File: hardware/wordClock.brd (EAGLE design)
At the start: 49.2 x 49.5 mm, 38 parts, among them J1 SPI_PRG, Q1 MOSFET-PCHANNELSMD, Q2 MOSFET-PCHANNELSMD, Q3 MOSFET-PCHANNELSMD, Q4 MOSFET-PCHANNELSMD, Q5 MOSFET-PCHANNELSMD, Q6 MOSFET-PCHANNELSMD, Q7 MOSFET-PCHANNELSMD, Q8 MOSFET-PCHANNELSMD, U2 TLC5940-NT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

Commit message: Fixed ERC errors and Fixed annotation breaks
Should be all good now, Got broken nets fixed, switched larger usb jack
for a micro.
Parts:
- C1: value (none) -> 10uF
- C2, C3, C4, C5, C8: value (none) -> .1uF
- C6, C7: value (none) -> 22uF
- JP1: value USB_PWR -> USB-MICROB; device SparkFun-Connectors:USB-B-PTH-VERTICAL -> SparkFun-Connectors:USB-MICROB
- SW1: value (none) -> HR
- SW2: value (none) -> MIN
- moved JP1 6.63 mm to (8.89, 3.17)
- renumbered HR to SW1, JP4 to COL, MIN to SW2, U$1 to ROW
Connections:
- removed net N$7: C6.2, C7.2, U3.21, U3.3, U3.5
- removed net ROW8: COL.9
- removed net ROW9: COL.10
- removed net SCI: U3.28
- net CE: now also U3.25
- net CLK: now also U3.12
- net GND: now also C6.2, C7.2, JP1.MT1, JP1.MT2, U3.21, U3.3, U3.5
- net IO: now also U3.26
- net SCL: now also U3.28
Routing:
- net N$7: track 5.08 -> 0.00 mm
- net GND: track 1.75 -> 6.83 mm

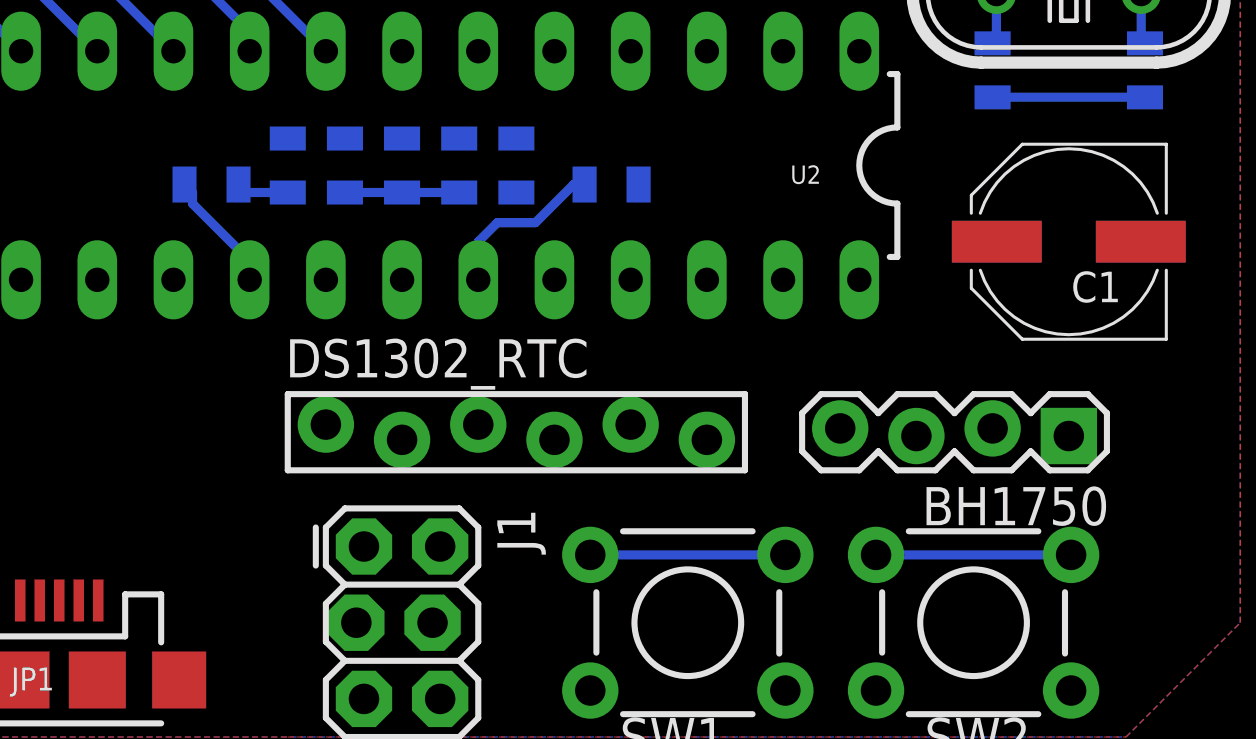
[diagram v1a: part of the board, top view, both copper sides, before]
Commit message: ALL ANNOTATION BREAKS FIXED
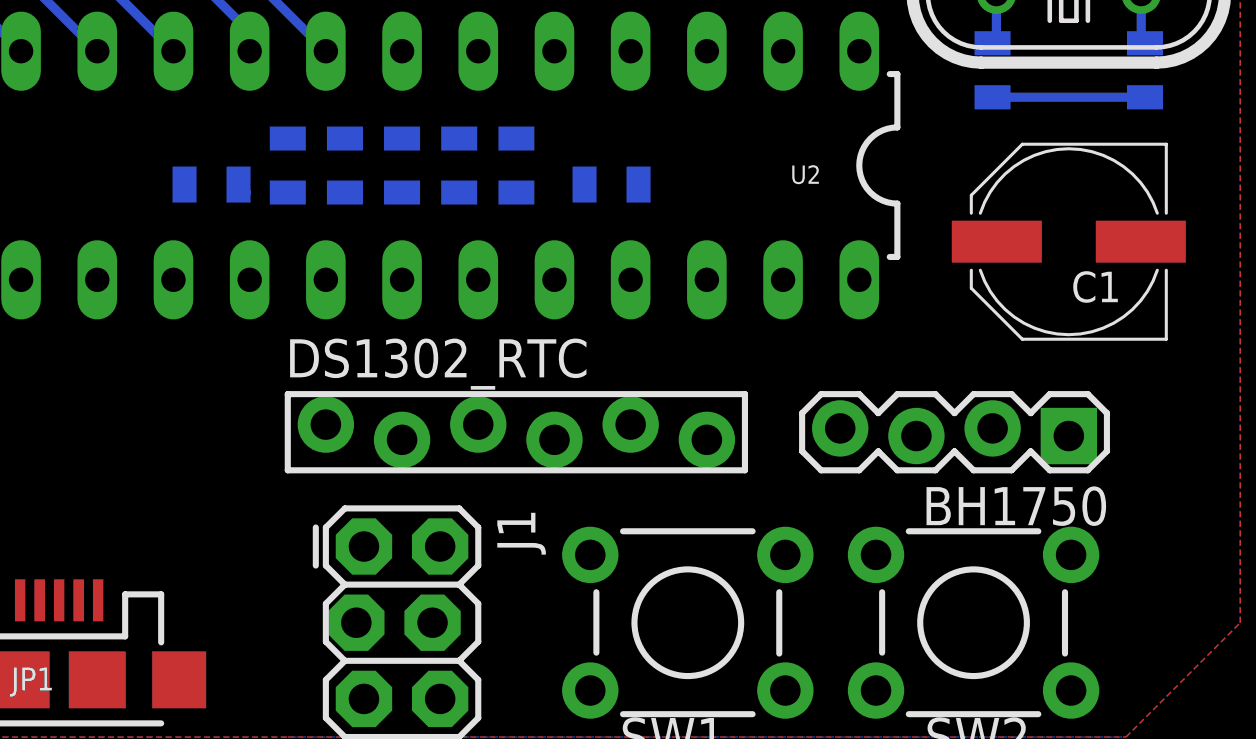
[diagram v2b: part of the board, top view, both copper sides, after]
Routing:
- net MIN: track 6.50 -> 0.00 mm
- net HR: track 6.50 -> 0.00 mm
- net BLANK: track 5.60 -> 0.00 mm
- net N$1: track 4.07 -> 0.00 mm
- net N$5: track 3.81 -> 0.00 mm
- net GND: track 6.83 -> 5.45 mm
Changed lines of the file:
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@@
 <vertex x="5.08" y="1.27"/>
 </polygon>
-<wire x1="16.51" y1="19.42" x2="15.135" y2="19.42" width="0.3048" layer="16"/>
+<wire x1="16.51" y1="19.42" x2="15.135" y2="19.42" width="0" layer="19" extent="1-16"/>
 <wire x1="15.135" y1="19.42" x2="14.87" y2="19.685" width="0.3048" layer="16"/>
 <contactref element="U3" pad="3"/>
@@
 <contactref element="R2" pad="1"/>
 <contactref element="U3" pad="14"/>
-<wire x1="26.405" y1="19.685" x2="26.035" y2="19.685" width="0.3048" layer="16"/>
-<wire x1="26.035" y1="19.685" x2="24.765" y2="18.415" width="0.3048" layer="16"/>
-<wire x1="24.765" y1="18.415" x2="23.495" y2="18.415" width="0.3048" layer="16"/>
-<wire x1="23.495" y1="18.415" x2="22.86" y2="17.78" width="0.3048" layer="16"/>
-<wire x1="22.86" y1="17.78" x2="22.86" y2="16.51" width="0.3048" layer="16"/>
-<wire x1="23.495" y1="18.415" x2="13.4874" y2="30.931" width="0" layer="19" extent="1-16"/>
+<wire x1="22.86" y1="16.51" x2="26.405" y2="19.685" width="0" layer="19" extent="16-16"/>
+<wire x1="13.4874" y1="30.931" x2="26.405" y2="19.685" width="0" layer="19" extent="1-16"/>
 </signal>
 <signal name="SIN">
@@
 <contactref element="SW1" pad="3"/>
 <contactref element="U3" pad="23"/>
-<wire x1="33.0962" y1="7.3406" x2="26.5938" y2="7.3406" width="0.3048" layer="16"/>
 <wire x1="26.5938" y1="7.3406" x2="19.78" y2="27.8384" width="0" layer="19" extent="1-1"/>
+<wire x1="33.0962" y1="7.3406" x2="26.5938" y2="7.3406" width="0" layer="19" extent="1-1"/>
 </signal>
 <signal name="MIN">
@@
 <contactref element="SW2" pad="3"/>
 <contactref element="U3" pad="24"/>
-<wire x1="42.6212" y1="7.3406" x2="36.1188" y2="7.3406" width="0.3048" layer="16"/>
-<wire x1="36.1188" y1="7.3406" x2="20.58" y2="27.8384" width="0" layer="19" extent="1-1"/>
+<wire x1="36.1188" y1="7.3406" x2="42.6212" y2="7.3406" width="0" layer="19" extent="1-1"/>
+<wire x1="20.58" y1="27.8384" x2="36.1188" y2="7.3406" width="0" layer="19" extent="1-1"/>
 </signal>
 <signal name="N$2">
@@
 <contactref element="U2" pad="20"/>
 <contactref element="R3" pad="1"/>
-<wire x1="15.24" y1="16.51" x2="15.24" y2="17.145" width="0.3048" layer="16"/>
-<wire x1="15.24" y1="17.145" x2="13.335" y2="19.05" width="0.3048" layer="16"/>
-<wire x1="13.335" y1="19.05" x2="13.335" y2="19.42" width="0.3048" layer="16"/>
-<wire x1="13.335" y1="19.42" x2="13.07" y2="19.685" width="0.3048" layer="16"/>
+<wire x1="13.07" y1="19.685" x2="15.24" y2="16.51" width="0" layer="19" extent="16-16"/>
 </signal>
 <signal name="MISO">
@@
 <wire x1="32.215" y1="40.005" x2="30.945" y2="41.275" width="0.3048" layer="16"/>
 </signal>
-<signal name="N$3">
+<signal name="N$5">
 <contactref element="C5" pad="2"/>
 <contactref element="C3" pad="2"/>
 <contactref element="C4" pad="2"/>
-<wire x1="18.415" y1="19.42" x2="20.32" y2="19.42" width="0.3048" layer="16"/>
-<wire x1="22.225" y1="19.42" x2="20.32" y2="19.42" width="0.3048" layer="16"/>
+<wire x1="20.32" y1="19.42" x2="22.225" y2="19.42" width="0" layer="19" extent="16-16"/>
+<wire x1="18.415" y1="19.42" x2="20.32" y2="19.42" width="0" layer="19" extent="16-16"/>
 </signal>
 </signals>

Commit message: Fixed floating nets
There was a floating net around the crystal, SCL was named SLI on a pin,
and various ERC errors fixed.
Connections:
- removed net N$5: C3.2, C4.2, C5.2
- net GND: now also C3.2, C4.2, C5.2
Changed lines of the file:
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@@
 <vertex x="5.08" y="1.27"/>
 </polygon>
-<wire x1="16.51" y1="19.42" x2="15.135" y2="19.42" width="0" layer="19" extent="1-16"/>
 <wire x1="15.135" y1="19.42" x2="14.87" y2="19.685" width="0.3048" layer="16"/>
 <contactref element="U3" pad="3"/>
@@
 <contactref element="JP1" pad="GND"/>
 <contactref element="JP1" pad="MT2"/>
+<contactref element="C5" pad="2"/>
+<contactref element="C3" pad="2"/>
+<contactref element="C4" pad="2"/>
 <wire x1="45.085" y1="22.595" x2="44.945" y2="17.78" width="0" layer="19" extent="1-16"/>
 <wire x1="40.005" y1="11.557" x2="44.945" y2="17.78" width="0" layer="19" extent="1-1"/>
@@
 <wire x1="26.5938" y1="2.8194" x2="33.0962" y2="2.8194" width="0" layer="19" extent="1-1"/>
 <wire x1="21.59" y1="2.54" x2="26.5938" y2="2.8194" width="0" layer="19" extent="1-1"/>
-<wire x1="22.86" y1="11.684" x2="21.59" y2="2.54" width="0" layer="19" extent="1-1"/>
-<wire x1="20.32" y1="16.51" x2="22.86" y2="11.684" width="0" layer="19" extent="1-1"/>
-<wire x1="24.13" y1="19.42" x2="20.32" y2="16.51" width="0" layer="19" extent="16-16"/>
-<wire x1="16.51" y1="19.42" x2="20.32" y2="16.51" width="0" layer="19" extent="16-16"/>
-<wire x1="18.18" y1="27.8384" x2="16.51" y2="19.42" width="0" layer="19" extent="1-16"/>
-<wire x1="18.98" y1="36.4236" x2="18.18" y2="27.8384" width="0" layer="19" extent="1-1"/>
-<wire x1="17.38" y1="36.4236" x2="18.98" y2="36.4236" width="0" layer="19" extent="1-1"/>
 <wire x1="12.89" y1="3.175" x2="21.59" y2="2.54" width="0" layer="19" extent="1-1"/>
 <wire x1="10.19" y1="5.825" x2="12.89" y2="3.175" width="0" layer="19" extent="1-1"/>
 <wire x1="4.89" y1="3.175" x2="10.19" y2="5.825" width="0" layer="19" extent="1-1"/>
+<wire x1="22.86" y1="11.684" x2="21.59" y2="2.54" width="0" layer="19" extent="1-1"/>
+<wire x1="20.32" y1="16.51" x2="22.86" y2="11.684" width="0" layer="19" extent="1-1"/>
+<wire x1="20.32" y1="19.42" x2="20.32" y2="16.51" width="0" layer="19" extent="16-16"/>
+<wire x1="22.225" y1="19.42" x2="20.32" y2="19.42" width="0" layer="19" extent="16-16"/>
+<wire x1="24.13" y1="19.42" x2="22.225" y2="19.42" width="0" layer="19" extent="16-16"/>
+<wire x1="18.415" y1="19.42" x2="20.32" y2="19.42" width="0" layer="19" extent="16-16"/>
+<wire x1="16.51" y1="19.42" x2="18.415" y2="19.42" width="0" layer="19" extent="16-16"/>
+<wire x1="15.135" y1="19.42" x2="16.51" y2="19.42" width="0" layer="19" extent="16-16"/>
+<wire x1="18.18" y1="27.8384" x2="18.415" y2="19.42" width="0" layer="19" extent="1-16"/>
+<wire x1="18.98" y1="36.4236" x2="18.18" y2="27.8384" width="0" layer="19" extent="1-1"/>
+<wire x1="17.38" y1="36.4236" x2="18.98" y2="36.4236" width="0" layer="19" extent="1-1"/>
 </signal>
 <signal name="CLK">
@@
 <wire x1="32.215" y1="40.005" x2="30.945" y2="41.275" width="0.3048" layer="16"/>
 </signal>
-<signal name="N$5">
-<contactref element="C5" pad="2"/>
-<contactref element="C3" pad="2"/>
-<contactref element="C4" pad="2"/>
-<wire x1="20.32" y1="19.42" x2="22.225" y2="19.42" width="0" layer="19" extent="16-16"/>
-<wire x1="18.415" y1="19.42" x2="20.32" y2="19.42" width="0" layer="19" extent="16-16"/>
-</signal>
 </signals>

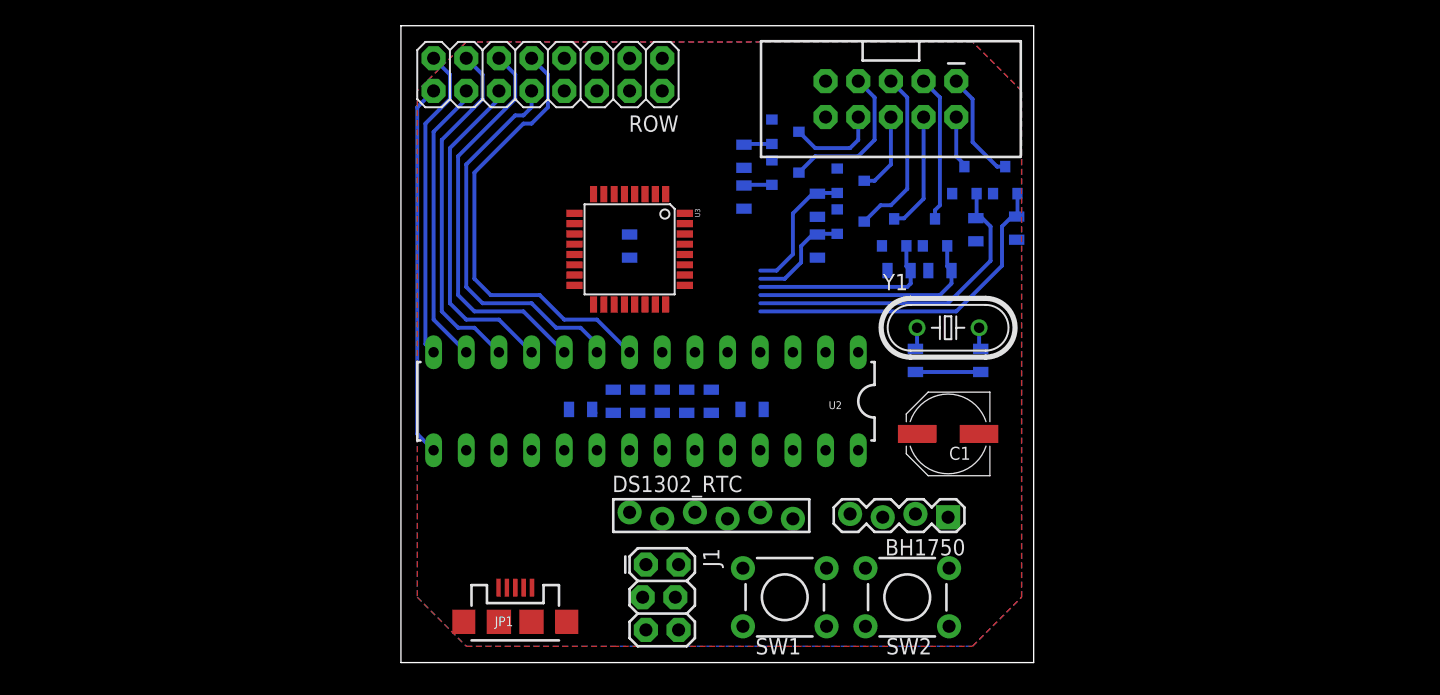
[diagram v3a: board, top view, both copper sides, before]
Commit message: Trying my hand at routing the board.
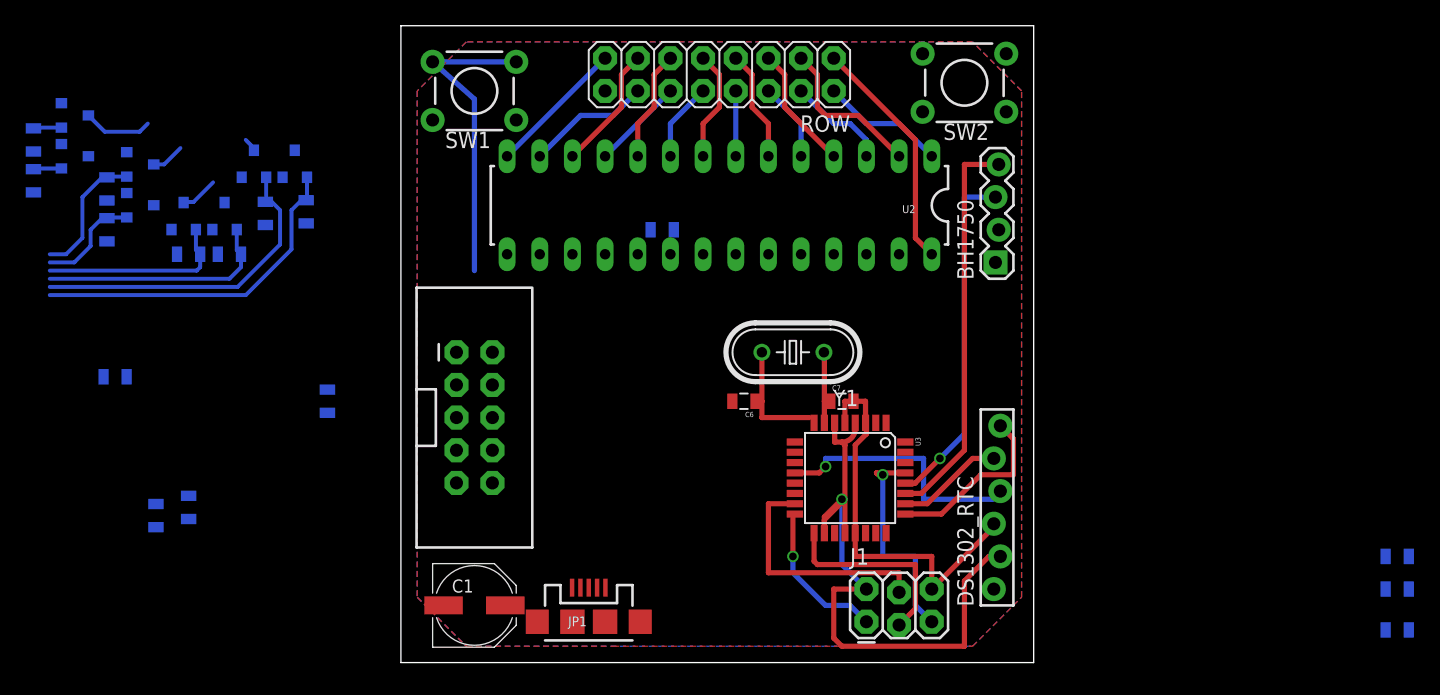
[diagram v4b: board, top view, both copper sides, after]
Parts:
- moved C3 56.5 mm to (77.5, 8.26), turned to 180 degrees
- moved C2 55.3 mm to (77.5, 5.71), turned to 180 degrees
- moved Q1 55.3 mm to (-8.26, 38.7)
- moved Q3 55.3 mm to (-13.7, 34.7)
- moved R10 55.3 mm to (-28.6, 37.5)
- moved R11 55.3 mm to (-28.6, 40.6)
- moved R5 55.3 mm to (-10.5, 34.9)
- moved R7 55.3 mm to (-16.5, 31.8)
- moved Q2 55.3 mm to (-11.4, 38.7)
- moved Q4 55.3 mm to (-16.9, 34.7)
- moved Q5 55.3 mm to (-20.3, 35.6)
- moved Q6 55.3 mm to (-20.3, 38.7)
- moved Q7 55.3 mm to (-25.4, 39.4)
- moved Q8 55.3 mm to (-25.4, 42.5)
- moved R4 55.3 mm to (-7.37, 35.1)
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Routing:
- net 5V: track 0.00 -> 50.9 mm, vias 0 -> 1
- net SDA: track 0.00 -> 30.9 mm
- net OUT15: track 29.0 -> 0.00 mm
- net SCL: track 0.00 -> 27.0 mm, vias 0 -> 1
- net OUT8: track 34.8 -> 8.67 mm
- net GND: track 5.45 -> 31.3 mm
- net OUT9: track 30.4 -> 6.13 mm
- net HR: track 0.00 -> 24.2 mm
- net OUT10: track 30.9 -> 8.67 mm
- net CLK: track 0.00 -> 20.3 mm, vias 0 -> 1
- net SIN: track 0.00 -> 19.1 mm
- net OUT11: track 26.0 -> 7.18 mm
- net OUT0: track 0.00 -> 18.4 mm
- net OUT12: track 27.3 -> 9.72 mm
- net RESET: track 0.00 -> 17.2 mm, vias 0 -> 1
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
